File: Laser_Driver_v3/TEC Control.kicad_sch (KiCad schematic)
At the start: 53 parts, among them Q10 IRF9540N, Q11 IRLB8721PBF, Q12 IRF9540N, Q3 IRF9540N, Q4 IRLB8721PBF, Q5 IRF9540N, Q6 IRLB8721PBF, Q8 IRLB8721PBF, U14 OPA192, U22 OPA551U, U23 OPA192, U24 OPA551U, U25 INA826, U27 INA826, U3 OPA192

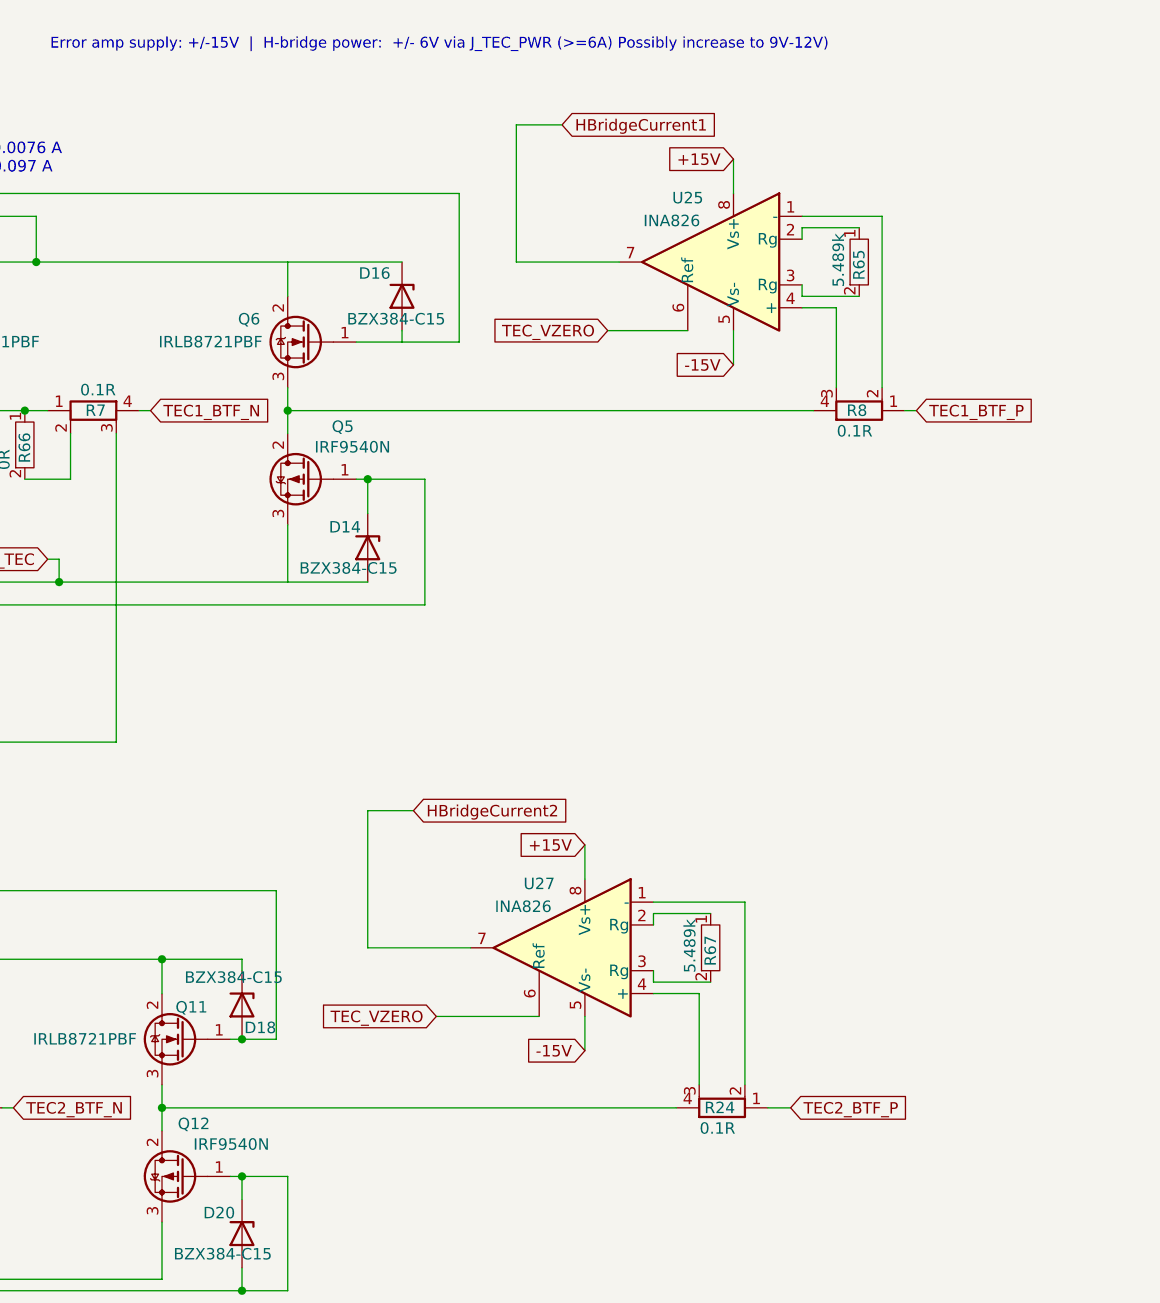
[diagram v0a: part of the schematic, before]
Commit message: Updated 5Vref and TEC and TEC controller
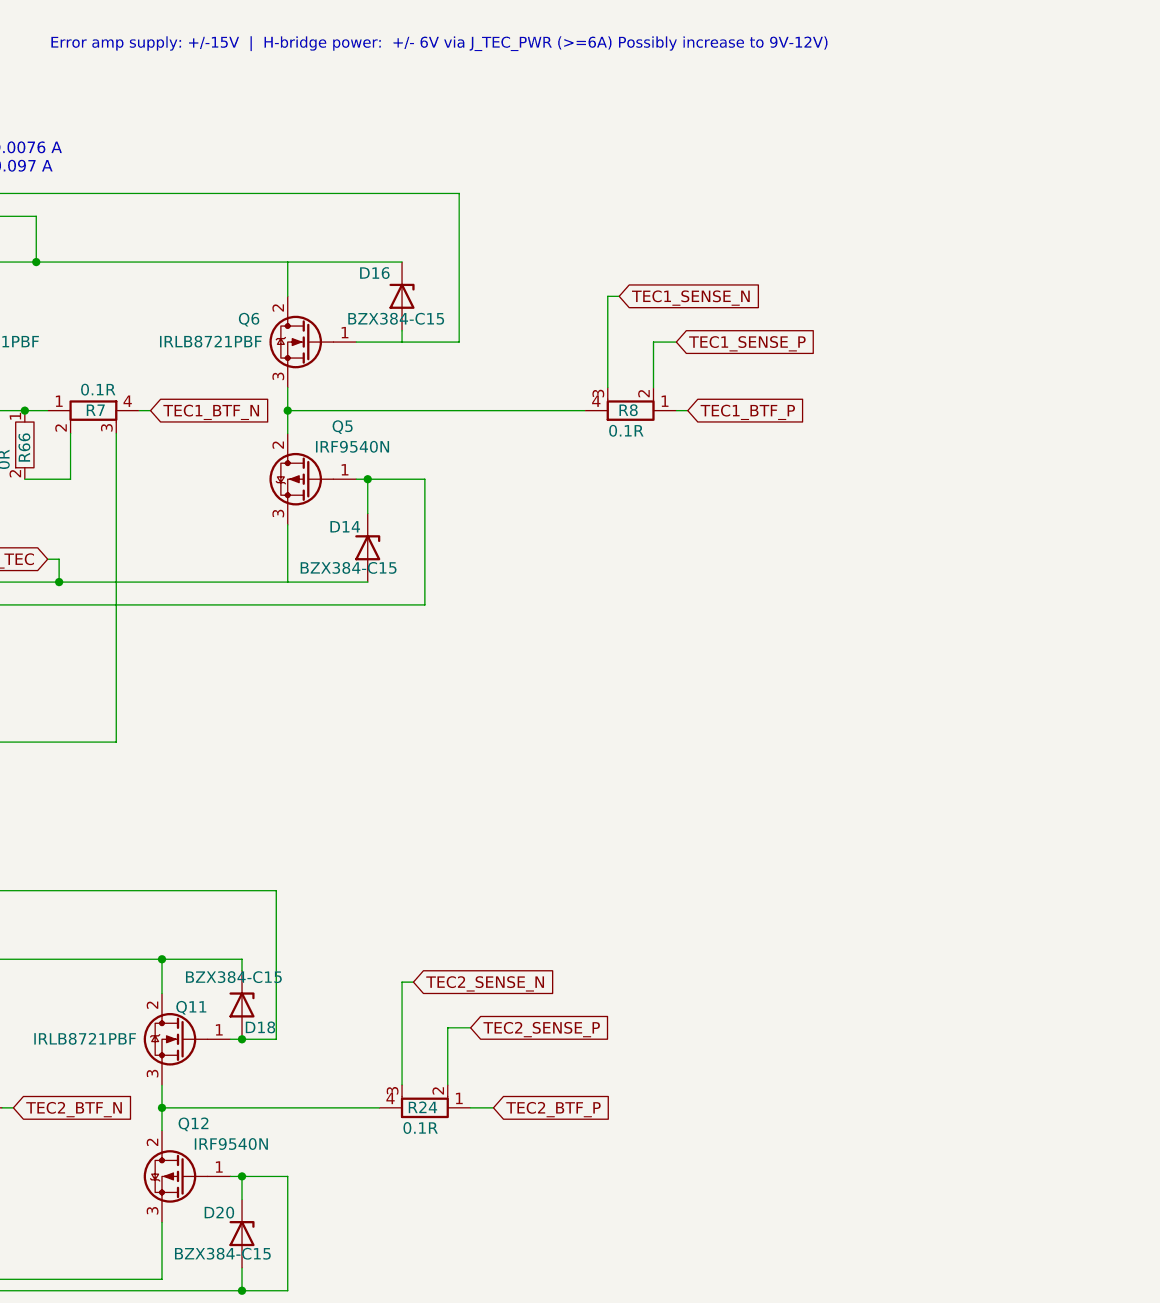
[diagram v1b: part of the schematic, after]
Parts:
- removed R65, R67: 5.489k, Resistor_SMD:R_0402_1005Metric, symbol Device:R
- removed U25, U27: INA826, Package_SO:SOIC-8_3.9x4.9mm_P1.27mm, symbol Amplifier_Instrumentation:INA821xD
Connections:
- net TEC2_SENSE_P: now reaches R24.2
- net TEC2_SENSE_N: now reaches R24.3
- net TEC1_SENSE_P: now reaches R8.2
- net TEC1_SENSE_N: now reaches R8.3
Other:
- moved on the sheet: R24, R8

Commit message: Renumbered schematics, corrections, power verified
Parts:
- renumbered C7 to C58, C6 to C59, D17 to D14, D19 to D15, D13 to D16, D15 to D17, D20 to D19, D14 to D20, D16 to D21, Q3 to Q10, Q6 to Q13, Q5 to Q14, Q8 to Q7, Q10 to Q8, Q4 to Q9, R55 to R38, R9 to R39, R16 to R40, R57 to R41, R35 to R42, R36 to R43, R58 to R44, R59 to R45, R39 to R46, R53 to R47, R60 to R48, R61 to R49, R62 to R50, R63 to R51, R64 to R52, R54 to R53, R50 to R54, R49 to R55, R51 to R56, R52 to R57, R68 to R58, R23 to R59, R66 to R60, R7 to R61, R24 to R62, R8 to R63, U14 to U18, U23 to U19, U3 to U20, U24 to U21
